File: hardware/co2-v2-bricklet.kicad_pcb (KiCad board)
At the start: 2 copper layers, 35 x 40 mm, 24 parts, among them P1 CON-SENSOR2, P2 DEBUG, P3 BOOT, U1 XMC1XXX24, U2 DRILL, U3 DRILL, U4 DRILL, U5 DRILL, U6 SCD30

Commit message: final pcb prototype design
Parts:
- added G***: LOGO, kicad-libraries:Logo_CoMCU, B.Cu at (113.8, 97.6)
- added VAL: CE_5mm, kicad-libraries:CE_5mm, B.Cu at (120.8, 97.6)
- added VAL: WEEE_7mm, kicad-libraries:WEEE_7mm, B.Cu at (106.8, 97.6)
- C2: footprint C0402E -> kicad-libraries:C0805
- C3: footprint C0402E -> kicad-libraries:C0603F
- R1, R2: footprint kicad-libraries:R0402F -> kicad-libraries:R0603F
- moved G*** 0.36 mm to (118.2, 79.9)
- moved R1 0.34 mm to (122.3, 117.4)
- moved R2 0.32 mm to (103.3, 117.4)
- moved C2 0.10 mm to (112.0, 111.7)
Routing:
- net +3.3VP: track 63.4 -> 80.8 mm, vias 8 -> 9
- net GND: track 39.5 -> 53.2 mm
- net Net-(D1-Pad2): track 0.00 -> 1.59 mm
- net SDA: track 35.6 -> 37.1 mm
- net Net-(R2-Pad1): track 27.8 -> 26.8 mm
- net Net-(P3-Pad2): track 5.08 -> 5.70 mm
- net Net-(P2-Pad1): track 8.81 -> 9.34 mm

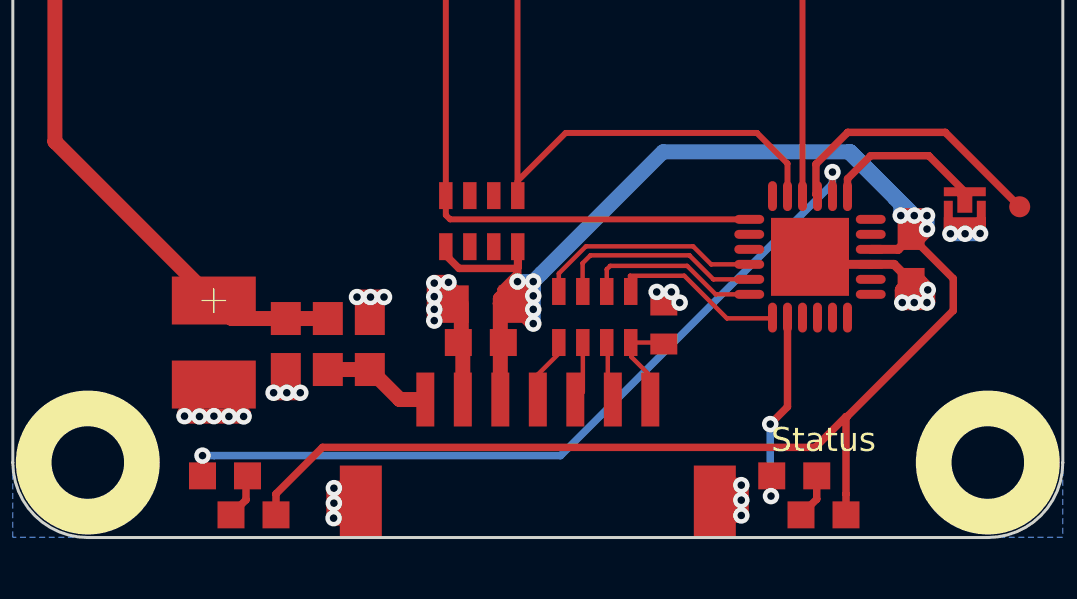
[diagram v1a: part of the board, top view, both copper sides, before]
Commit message: added "info" to silkscreen and changed the led positions
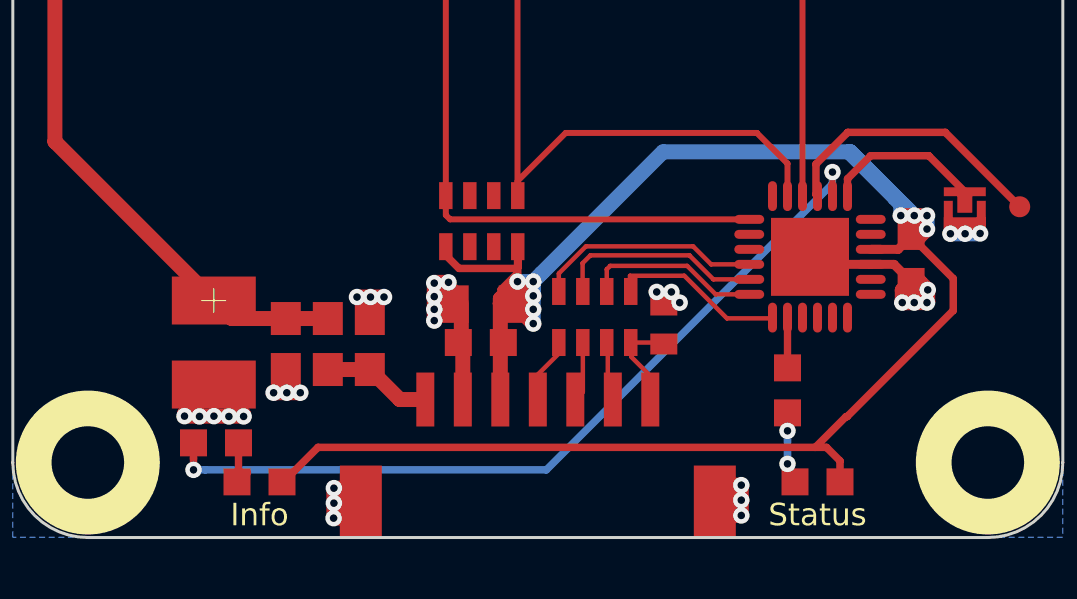
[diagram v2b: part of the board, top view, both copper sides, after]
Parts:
- moved R1 2.86 mm to (122.1, 114.5), turned to 270 degrees
- moved R2 1.14 mm to (103.0, 116.3)
- moved D1 1.12 mm to (123.1, 117.6)
- moved D2 1.12 mm to (104.5, 117.6)
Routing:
- net Net-(R1-Pad1): track 6.99 -> 1.67 mm, vias 2 -> 0
- net +3.3VP: track 80.8 -> 77.8 mm
- net Net-(D1-Pad2): track 1.59 -> 2.40 mm, vias 0 -> 2
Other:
- board text added: "Info"

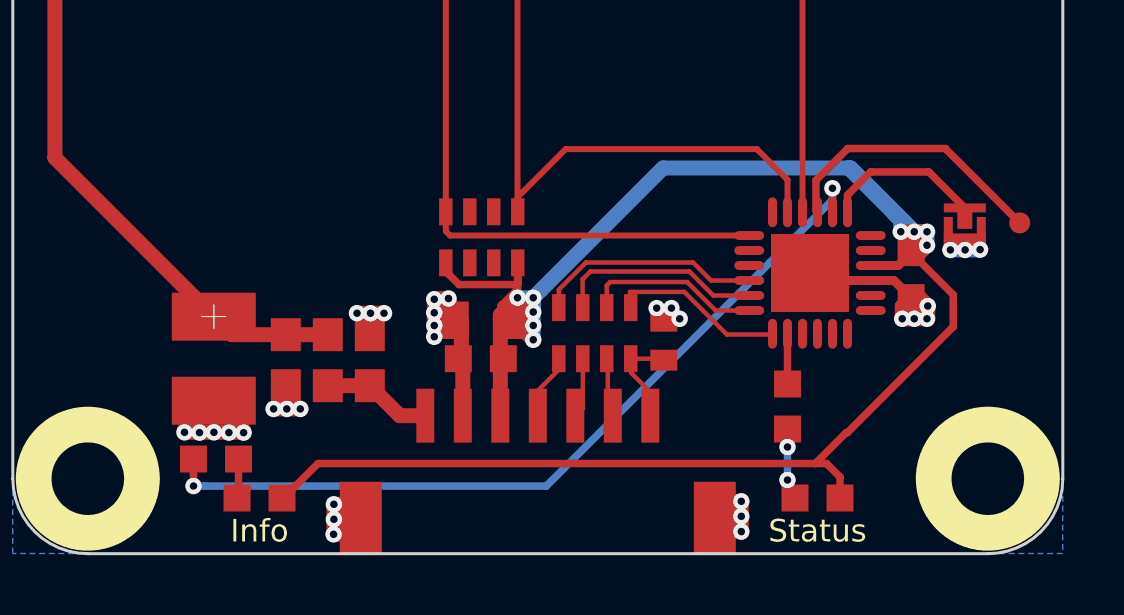
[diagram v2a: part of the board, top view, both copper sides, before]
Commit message: changed led pin and routed new trace on front
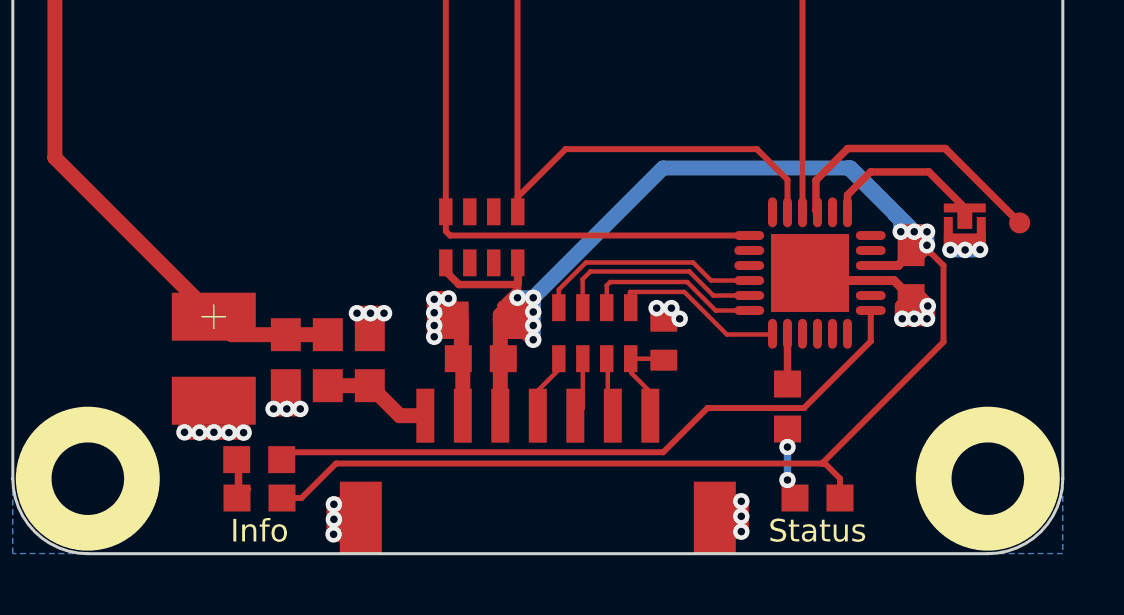
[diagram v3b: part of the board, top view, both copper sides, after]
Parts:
- moved R2 1.44 mm to (104.5, 116.3), turned to 180 degrees
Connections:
- U1 pad 14: Net-(R2-Pad1) -> Net-(U1-Pad14)
- U1 pad 7: Net-(U1-Pad7) -> Net-(R2-Pad1)
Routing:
- net Net-(R2-Pad1): track 27.3 -> 22.3 mm, vias 2 -> 0
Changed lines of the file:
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@@
     (thickness 1.6)
     (drawings 12)
-    (tracks 340)
+    (tracks 334)
     (zones 0)
     (modules 27)
@@
   )
   (setup
-    (last_trace_width 0.25)
+    (last_trace_width 0.2)
     (user_trace_width 0.2)
     (user_trace_width 0.25)
@@
   (net 26 "Net-(U1-Pad5)")
   (net 27 "Net-(U1-Pad6)")
-  (net 28 "Net-(U1-Pad7)")
-  (net 29 "Net-(U1-Pad8)")
-  (net 30 "Net-(U1-Pad11)")
-  (net 31 "Net-(U1-Pad12)")
-  (net 32 "Net-(U1-Pad18)")
-  (net 33 "Net-(U1-Pad20)")
-  (net 34 "Net-(U1-Pad21)")
-  (net 35 "Net-(U6-Pad6)")
-  (net 36 "Net-(R1-Pad1)")
-  (net 37 "Net-(R2-Pad1)")
+  (net 28 "Net-(U1-Pad8)")
+  (net 29 "Net-(U1-Pad11)")
+  (net 30 "Net-(U1-Pad12)")
+  (net 31 "Net-(U1-Pad18)")
+  (net 32 "Net-(U1-Pad20)")
+  (net 33 "Net-(U1-Pad21)")
+  (net 34 "Net-(U6-Pad6)")
+  (net 35 "Net-(R1-Pad1)")
+  (net 36 "Net-(R2-Pad1)")
+  (net 37 "Net-(U1-Pad14)")
   (net_class Default "This is the default net class."
     (clearance 0.15)
@@
     (add_net "Net-(U1-Pad11)")
     (add_net "Net-(U1-Pad12)")
+    (add_net "Net-(U1-Pad14)")
     (add_net "Net-(U1-Pad18)")
     (add_net "Net-(U1-Pad20)")
@@
     (add_net "Net-(U1-Pad5)")
     (add_net "Net-(U1-Pad6)")
-    (add_net "Net-(U1-Pad7)")
     (add_net "Net-(U1-Pad8)")
     (add_net "Net-(U6-Pad6)")
@@
   )
   (module kicad-libraries:R0603F (layer F.Cu)
-    (at 103.05 116.3)
+    (at 104.49 116.32 180)
     (attr smd)
-    (fp_text reference R2 (at 0.05 0.225) (layer F.Fab)
+    (fp_text reference R2 (at 0.05 0.225 180) (layer F.Fab)
       (effects (font (size 0.2 0.2) (thickness 0.05)))
     )
-    (fp_text value 1k (at 0.05 -0.375) (layer F.Fab)
+    (fp_text value 1k (at 0.05 -0.375 180) (layer F.Fab)
       (effects (font (size 0.2 0.2) (thickness 0.05)))
     )
@@
     (fp_line (start 1.45034 -0.65024) (end 1.45034 0.65024) (layer F.Fab) (width 0.001))
     (fp_line (start -1.45034 -0.65024) (end 1.45034 -0.65024) (layer F.Fab) (width 0.001))
-    (pad 2 smd rect (at 0.75 0) (size 0.9 0.9) (layers F.Cu F.Paste F.Mask)
+    (pad 2 smd rect (at 0.75 0 180) (size 0.9 0.9) (layers F.Cu F.Paste F.Mask)
       (net 7 "Net-(D2-Pad2)"))
-    (pad 1 smd rect (at -0.75 0) (size 0.9 0.9) (layers F.Cu F.Paste F.Mask)
-      (net 37 "Net-(R2-Pad1)"))
+    (pad 1 smd rect (at -0.75 0 180) (size 0.9 0.9) (layers F.Cu F.Paste F.Mask)
+      (net 36 "Net-(R2-Pad1)"))
     (model Resistors_SMD/R_0603.wrl
       (at (xyz 0 0 0))
@@
       (net 6 "Net-(D1-Pad2)"))
     (pad 1 smd rect (at -0.75 0 270) (size 0.9 0.9) (layers F.Cu F.Paste F.Mask)
-      (net 36 "Net-(R1-Pad1)"))
+      (net 35 "Net-(R1-Pad1)"))
     (model Resistors_SMD/R_0603.wrl
       (at (xyz 0 0 0))
@@
       (net 16 S-MISO))
     (pad 2 smd oval (at -2.025 -0.75 90) (size 1 0.3) (layers F.Cu F.Paste F.Mask)
-      (net 36 "Net-(R1-Pad1)"))
+      (net 35 "Net-(R1-Pad1)"))
     (pad 3 smd oval (at -2.025 -0.25 90) (size 1 0.3) (layers F.Cu F.Paste F.Mask)
       (net 24 "Net-(U1-Pad3)"))
@@
       (net 27 "Net-(U1-Pad6)"))
     (pad 7 smd oval (at -1.25 2.025 180) (size 1 0.3) (layers F.Cu F.Paste F.Mask)
-      (net 28 "Net-(U1-Pad7)"))
+      (net 36 "Net-(R2-Pad1)"))
     (pad 8 smd oval (at -0.75 2.025 180) (size 1 0.3) (layers F.Cu F.Paste F.Mask)
-      (net 29 "Net-(U1-Pad8)"))
+      (net 28 "Net-(U1-Pad8)"))
     (pad 9 smd oval (at -0.25 2.025 180) (size 1 0.3) (layers F.Cu F.Paste F.Mask)
       (net 2 GND))
@@
       (net 3 +3.3VP))
     (pad 11 smd oval (at 0.75 2.025 180) (size 1 0.3) (layers F.Cu F.Paste F.Mask)
-      (net 30 "Net-(U1-Pad11)"))
+      (net 29 "Net-(U1-Pad11)"))
     (pad 12 smd oval (at 1.25 2.025 180) (size 1 0.3) (layers F.Cu F.Paste F.Mask)
-      (net 31 "Net-(U1-Pad12)"))
+      (net 30 "Net-(U1-Pad12)"))
     (pad 13 smd oval (at 2.025 1.25 90) (size 1 0.3) (layers F.Cu F.Paste F.Mask)
       (net 12 "Net-(P3-Pad2)"))
     (pad 14 smd oval (at 2.025 0.75 90) (size 1 0.3) (layers F.Cu F.Paste F.Mask)
-      (net 37 "Net-(R2-Pad1)"))
+      (net 37 "Net-(U1-Pad14)"))
     (pad 15 smd oval (at 2.025 0.25 90) (size 1 0.3) (layers F.Cu F.Paste F.Mask)
       (net 11 "Net-(P2-Pad1)"))
@@
       (net 17 SDA))
     (pad 18 smd oval (at 2.025 -1.25 90) (size 1 0.3) (layers F.Cu F.Paste F.Mask)
-      (net 32 "Net-(U1-Pad18)"))
+      (net 31 "Net-(U1-Pad18)"))
     (pad 19 smd oval (at 1.25 -2.025 180) (size 1 0.3) (layers F.Cu F.Paste F.Mask)
       (net 20 SCL))
     (pad 20 smd oval (at 0.75 -2.025 180) (size 1 0.3) (layers F.Cu F.Paste F.Mask)
-      (net 33 "Net-(U1-Pad20)"))
+      (net 32 "Net-(U1-Pad20)"))
     (pad 21 smd oval (at 0.25 -2.025 180) (size 1 0.3) (layers F.Cu F.Paste F.Mask)
-      (net 34 "Net-(U1-Pad21)"))
+      (net 33 "Net-(U1-Pad21)"))
     (pad 22 smd oval (at -0.25 -2.025 180) (size 1 0.3) (layers F.Cu F.Paste F.Mask)
       (net 13 S-CS))
@@
       (net 2 GND))
     (pad 6 thru_hole circle (at -14.1 -1.4 180) (size 1.8 1.8) (drill 1) (layers *.Cu *.Mask)
-      (net 35 "Net-(U6-Pad6)"))
+      (net 34 "Net-(U6-Pad6)"))
     (pad 5 thru_hole circle (at -11.56 -1.4 180) (size 1.8 1.8) (drill 1) (layers *.Cu *.Mask)
       (net 23 RDY))
@@
   (segment (start 125.79 109.85) (end 124.875 109.85) (width 0.3) (layer F.Cu) (net 3))
   (segment (start 126.22 109.42) (end 125.79 109.85) (width 0.3) (layer F.Cu) (net 3))
-  (segment (start 127.625 110.825) (end 126.22 109.42) (width 0.25) (layer F.Cu) (net 3))
-  (segment (start 106.45 116.45) (end 123.025 116.45) (width 0.25) (layer F.Cu) (net 3))
-  (segment (start 124.05 115.425) (end 124.089004 115.425) (width 0.25) (layer F.Cu) (net 3))
-  (segment (start 124.089004 115.425) (end 127.625 111.889004) (width 0.25) (layer F.Cu) (net 3))
-  (segment (start 105.5 117.4) (end 106.45 116.45) (width 0.25) (layer F.Cu) (net 3))
-  (segment (start 127.625 111.889004) (end 127.625 110.825) (width 0.25) (layer F.Cu) (net 3))
-  (segment (start 123.025 116.45) (end 124.05 115.425) (width 0.25) (layer F.Cu) (net 3))
-  (segment (start 123.4 116.45) (end 123.025 116.45) (width 0.25) (layer F.Cu) (net 3))
-  (segment (start 123.85 116.9) (end 123.4 116.45) (width 0.25) (layer F.Cu) (net 3))
-  (segment (start 123.85 117.6) (end 123.85 116.9) (width 0.25) (layer F.Cu) (net 3))
+  (segment (start 123.25 116.45) (end 107.05 116.45) (width 0.2) (layer F.Cu) (net 3))
+  (segment (start 105.9 117.6) (end 105.25 117.6) (width 0.2) (layer F.Cu) (net 3))
+  (segment (start 107.05 116.45) (end 105.9 117.6) (width 0.2) (layer F.Cu) (net 3))
+  (segment (start 127.300001 112.399999) (end 123.25 116.45) (width 0.2) (layer F.Cu) (net 3))
+  (segment (start 127.300001 109.850001) (end 127.300001 112.399999) (width 0.2) (layer F.Cu) (net 3))
+  (segment (start 126.87 109.42) (end 127.300001 109.850001) (width 0.2) (layer F.Cu) (net 3))
+  (segment (start 126.22 109.42) (end 126.87 109.42) (width 0.2) (layer F.Cu) (net 3))
+  (segment (start 123.85 116.95) (end 123.85 117.6) (width 0.2) (layer F.Cu) (net 3))
+  (segment (start 123.35 116.45) (end 123.85 116.95) (width 0.2) (layer F.Cu) (net 3))
+  (segment (start 123.25 116.45) (end 123.35 116.45) (width 0.2) (layer F.Cu) (net 3))
   (segment (start 109.177192 114.855794) (end 108.177192 113.855794) (width 0.5) (layer F.Cu) (net 4))
   (segment (start 110.027192 114.855794) (end 109.177192 114.855794) (width 0.5) (layer F.Cu) (net 4))
@@
   (segment (start 122.6 108.075) (end 122.6 100.618602) (width 0.2) (layer F.Cu) (net 23) (status 400000))
   (segment (start 122.6 100.618602) (end 107.837192 85.855794) (width 0.2) (layer F.Cu) (net 23) (status 800000))
-  (segment (start 122.1 112.125) (end 122.1 113.8) (width 0.25) (layer F.Cu) (net 36))
-  (via (at 123.598434 107.274295) (size 0.55) (drill 0.25) (layers F.Cu B.Cu) (net 37))
+  (segment (start 122.1 112.125) (end 122.1 113.8) (width 0.25) (layer F.Cu) (net 35))
   (segment (start 123.598434 108.073434) (end 123.6 108.075) (width 0.2) (layer F.Cu) (net 37))
-  (segment (start 123.598434 107.274295) (end 123.598434 108.073434) (width 0.2) (layer F.Cu) (net 37))
-  (segment (start 123.622729 107.25) (end 123.598434 107.274295) (width 0.2) (layer B.Cu) (net 37))
-  (segment (start 123.65 107.25) (end 123.622729 107.25) (width 0.2) (layer B.Cu) (net 37))
-  (via (at 102.300004 117.2) (size 0.55) (drill 0.25) (layers F.Cu B.Cu) (net 37))
-  (segment (start 114.061637 117.2) (end 102.688912 117.2) (width 0.25) (layer B.Cu) (net 37))
-  (segment (start 102.688912 117.2) (end 102.300004 117.2) (width 0.25) (layer B.Cu) (net 37))
-  (segment (start 123.598434 107.663203) (end 114.061637 117.2) (width 0.25) (layer B.Cu) (net 37))
-  (segment (start 123.598434 107.274295) (end 123.598434 107.663203) (width 0.25) (layer B.Cu) (net 37))
-  (segment (start 102.300004 116.811092) (end 102.300004 117.2) (width 0.25) (layer F.Cu) (net 37))
-  (segment (start 102.3 116.4) (end 102.300004 116.400004) (width 0.25) (layer F.Cu) (net 37))
-  (segment (start 102.300004 116.400004) (end 102.300004 116.811092) (width 0.25) (layer F.Cu) (net 37))
+  (segment (start 117.957998 116.07499) (end 105.59501 116.07499) (width 0.2) (layer F.Cu) (net 36))
+  (segment (start 119.432989 114.599999) (end 117.957998 116.07499) (width 0.2) (layer F.Cu) (net 36))
+  (segment (start 122.650003 114.599999) (end 119.432989 114.599999) (width 0.2) (layer F.Cu) (net 36))
+  (segment (start 124.875 111.35) (end 124.875 112.375002) (width 0.2) (layer F.Cu) (net 36))
+  (segment (start 124.875 112.375002) (end 122.650003 114.599999) (width 0.2) (layer F.Cu) (net 36))
+  (segment (start 105.59501 116.07499) (end 105.29 116.38) (width 0.2) (layer F.Cu) (net 36))
   (zone (net 2) (net_name GND) (layer B.Cu) (hatch edge 0.508)
     (connect_pads (clearance 0.508))
